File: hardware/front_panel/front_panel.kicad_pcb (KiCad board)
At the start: 2 copper layers, 200 x 124 mm, 0 parts

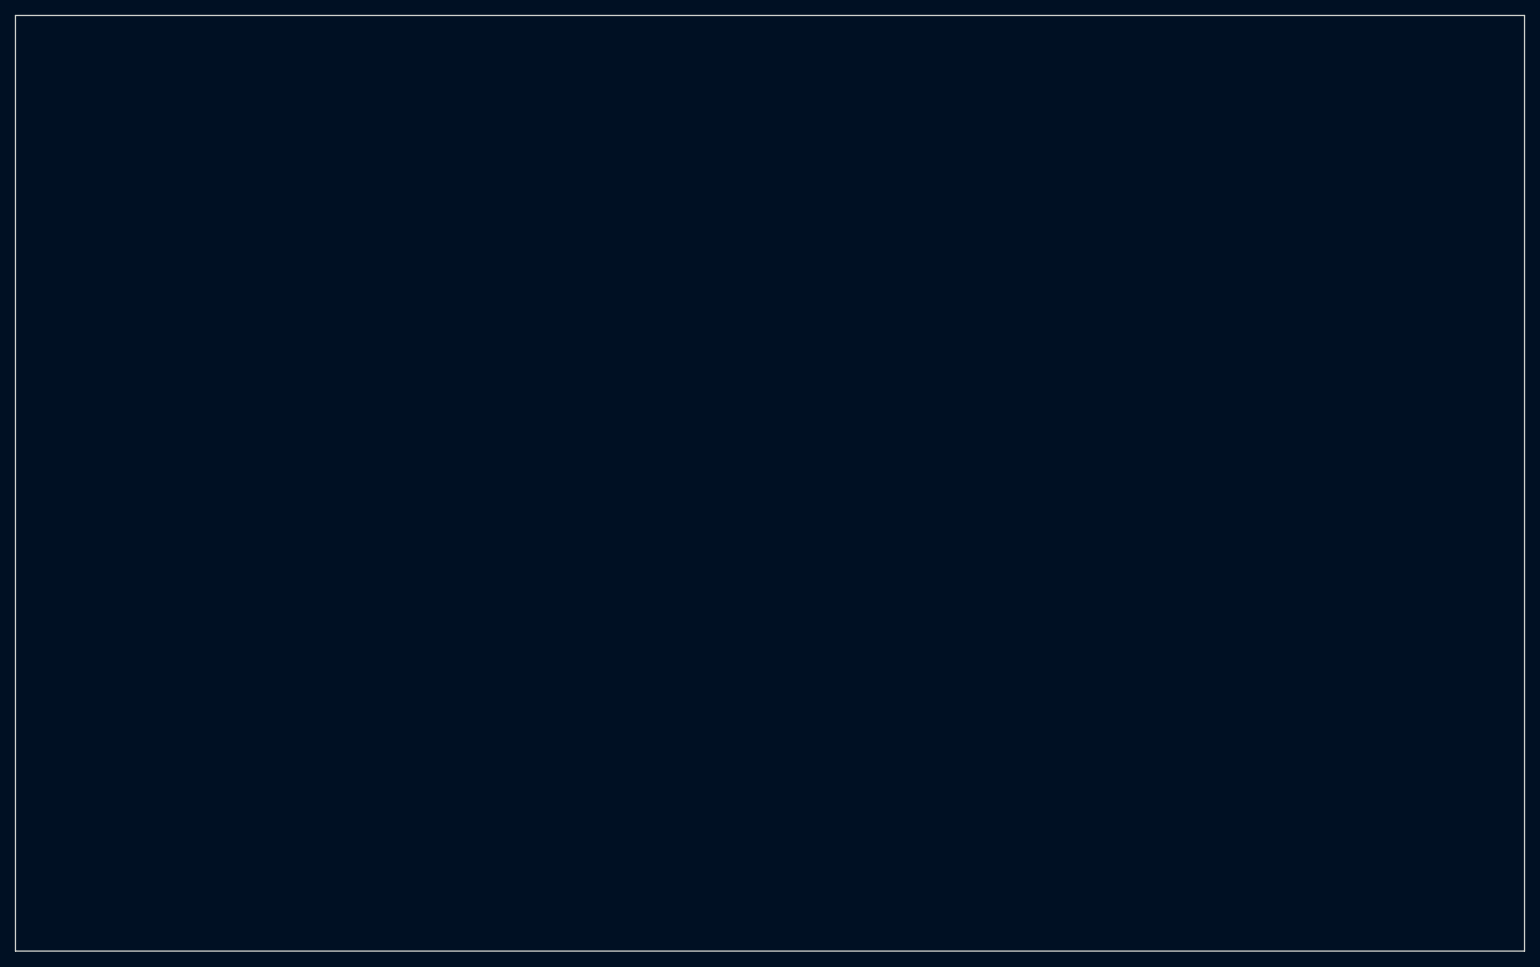
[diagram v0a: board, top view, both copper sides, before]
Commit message: front panel connector placement and lcd
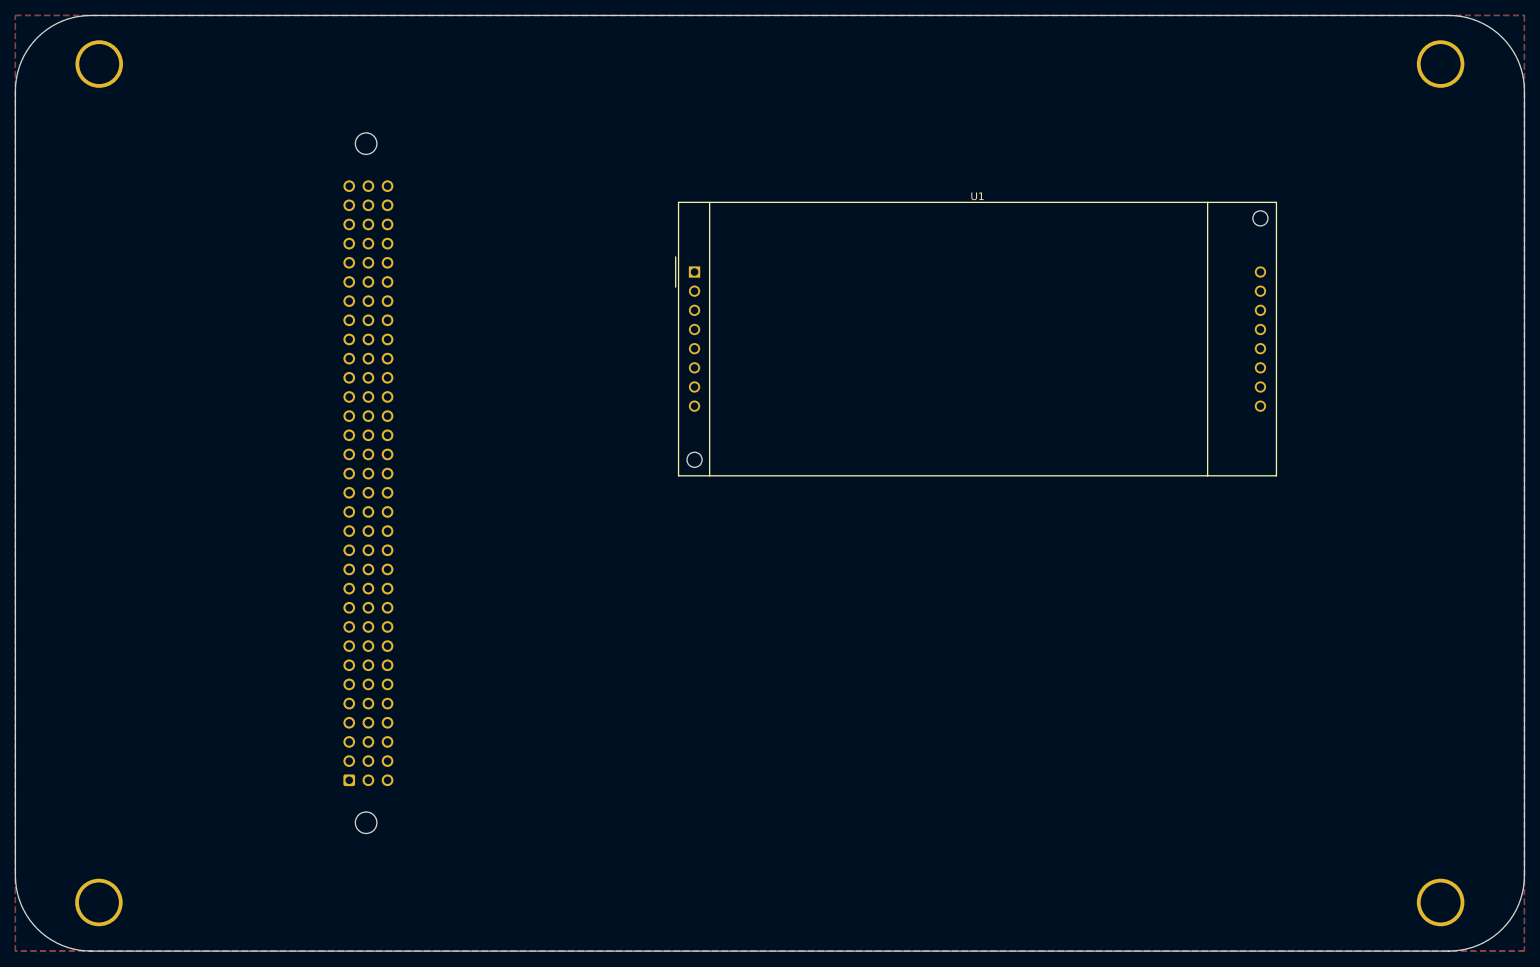
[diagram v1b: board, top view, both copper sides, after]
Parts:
- added H1: MountingHole, rails:m5-close, B.Cu at (200.9, 129.6)
- added H2: MountingHole, rails:m5-close, B.Cu at (200.9, 18.4)
- added H3: MountingHole, rails:m5-close, B.Cu at (23.1, 18.4)
- added H4: MountingHole, rails:m5-close, B.Cu at (23.1, 129.6)
- added J1: C96ABC, Connector_DIN:DIN41612_C_3x32_Female_Vertical_THT, B.Cu at (56.2, 113.4)
- added U1: NHD-0420H1Z, Display:NHD-0420H1Z, F.Cu at (102.0, 46.0)
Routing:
- added copper zone on B.Cu, net GND
- added copper zone on F.Cu, net VCC
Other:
- outline, holes or cut-outs redrawn

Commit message: FP WIP
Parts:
- added D1: LED, LED_THT:LED_D5.0mm, F.Cu at (139.9, 30.5)
- added H5: MountingHole, rails:m5-close, F.Cu at (112.0, 18.4)
- added H6: MountingHole, rails:m5-close, F.Cu at (112.0, 129.6)
- added JP1: Conn_02x01, Connector_PinHeader_2.54mm:PinHeader_1x02_P2.54mm_Vertical, B.Cu at (162.8, 129.6)
- added JP2: Conn_01x03_Male, Connector_PinHeader_2.54mm:PinHeader_1x03_P2.54mm_Vertical, B.Cu at (170.4, 127.0)
- added JP3: Conn_02x01, Connector_PinHeader_2.54mm:PinHeader_1x02_P2.54mm_Vertical, B.Cu at (155.1, 129.6)
- added JP4: Conn_02x01, Connector_PinHeader_2.54mm:PinHeader_1x02_P2.54mm_Vertical, B.Cu at (178.0, 127.0)
- added JP5: Conn_02x01, Connector_PinHeader_2.54mm:PinHeader_1x02_P2.54mm_Vertical, B.Cu at (165.3, 18.4)
- added JP6: Conn_02x01, Connector_PinHeader_2.54mm:PinHeader_1x02_P2.54mm_Vertical, B.Cu at (139.9, 15.9)
- added JP7: Conn_02x01, Connector_PinHeader_2.54mm:PinHeader_1x02_P2.54mm_Vertical, B.Cu at (152.6, 15.9)
- added JP8: Conn_02x01, Connector_PinHeader_2.54mm:PinHeader_1x02_P2.54mm_Vertical, B.Cu at (178.0, 15.9)
- added JP9: Conn_01x03_Male, Connector_PinHeader_2.54mm:PinHeader_1x03_P2.54mm_Vertical, B.Cu at (147.5, 132.1)
- added R1: 100k, Potentiometer_THT:Potentiometer_TT_P0915N, F.Cu at (160.2, 109.2)
- added RN1: R_Network08, Resistor_THT:R_Array_SIP9, F.Cu at (79.2, 19.3)
- added SW7: SW_DIP_x08, Button_Switch_THT:SW_DIP_SPSTx08_Piano_10.8x21.88mm_W7.62mm_P2.54mm, F.Cu at (81.8, 31.4)
- added U2: 74HC688, Package_DIP:DIP-20_W7.62mm_Socket, F.Cu at (73.9, 39.6)
- moved U1 15.8 mm to (117.7, 48.0)
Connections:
- J1 pad C24: Net-(J1-PadC24) -> /bd5
- J1 pad C25: Net-(J1-PadC25) -> /bd4
- J1 pad C26: Net-(J1-PadC26) -> /bd3
- J1 pad C27: Net-(J1-PadC27) -> /bd2
- J1 pad C28: Net-(J1-PadC28) -> /bd1
- J1 pad C29: Net-(J1-PadC29) -> /bd0
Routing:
- net Net-(RN1-Pad6): track 0.00 -> 52.5 mm
- net Net-(RN1-Pad5): track 0.00 -> 50.3 mm
- net Net-(RN1-Pad7): track 0.00 -> 49.2 mm
- net Net-(RN1-Pad8): track 0.00 -> 45.9 mm
- net Net-(RN1-Pad4): track 0.00 -> 43.1 mm
- net Net-(RN1-Pad9): track 0.00 -> 42.6 mm
- net Net-(RN1-Pad3): track 0.00 -> 35.8 mm
- net Net-(RN1-Pad2): track 0.00 -> 28.7 mm
- net /bd5: track 0.00 -> 28.5 mm
- net /bd4: track 0.00 -> 24.4 mm
- net Net-(JP1-Pad1): track 0.00 -> 21.4 mm
- net Net-(JP1-Pad2): track 0.00 -> 17.7 mm
- net /bd3: track 0.00 -> 15.7 mm
- net /bd2: track 0.00 -> 14.6 mm
- net /bd1: track 0.00 -> 13.6 mm
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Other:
- board text added: "+"
- board text added: "-"
- board text added: "555_ADJ"
- board text added: "555_STEP"
- board text added: "AST_MONO_SW"
- board text added: "CLK_EN"
- board text added: "CLK_SEL"
- board text added: "POWER_LED"
- board text added: "POWER_SW"
- board text added: "RESET_SW"
- board text added: "SB_LED"

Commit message: front panel: nhd-0440wh 4x40 panel
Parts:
- removed U1: NHD-0420H1Z, Display:NHD-0420H1Z
- added U3: NHD-0440WH, nhd-0040wh:NHD-0040WH, F.Cu at (18.0, 27.6)
- moved RN1 101.7 mm to (28.2, 107.3)
- moved SW7 101.7 mm to (30.8, 119.4)
- moved U2 75.3 mm to (15.8, 87.6)
- moved R1 11.8 mm to (160.3, 121.1)
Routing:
- net /bd3: track 15.7 -> 76.8 mm
- net /bd2: track 14.6 -> 74.3 mm
- net /bd1: track 13.6 -> 71.9 mm
- net /bd0: track 12.6 -> 69.3 mm
- net /bd4: track 24.4 -> 79.9 mm
- net /bd5: track 28.5 -> 73.0 mm
- net Net-(RN1-Pad6): track 52.5 -> 23.4 mm
- net Net-(RN1-Pad7): track 49.2 -> 26.4 mm
- net Net-(RN1-Pad5): track 50.3 -> 31.7 mm
- net Net-(RN1-Pad8): track 45.9 -> 33.1 mm
- net Net-(JP1-Pad1): track 21.4 -> 9.54 mm
- net Net-(JP1-Pad2): track 17.7 -> 5.96 mm
- net Net-(RN1-Pad4): track 43.1 -> 33.5 mm
- net Net-(RN1-Pad2): track 28.7 -> 37.1 mm
- net Net-(RN1-Pad9): track 42.6 -> 39.9 mm
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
